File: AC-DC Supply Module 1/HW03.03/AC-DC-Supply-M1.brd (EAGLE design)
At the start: 125 x 100 mm, 76 parts, among them IC101 LD1117S33TR, IC102 TPS54202DDCR, IC103 TPS54202DDCR, IC104 MAX764CSA+, M101 M_HOLE_3M, M102 M_HOLE_3M, M103 M_HOLE_3M, M104 M_HOLE_3M, U101 TL431AQDBZR,215NEXPERIA_TL431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, X1 726386-2, X2 726386-2, X3 MOLEX_206832-0601MOLEX_206832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

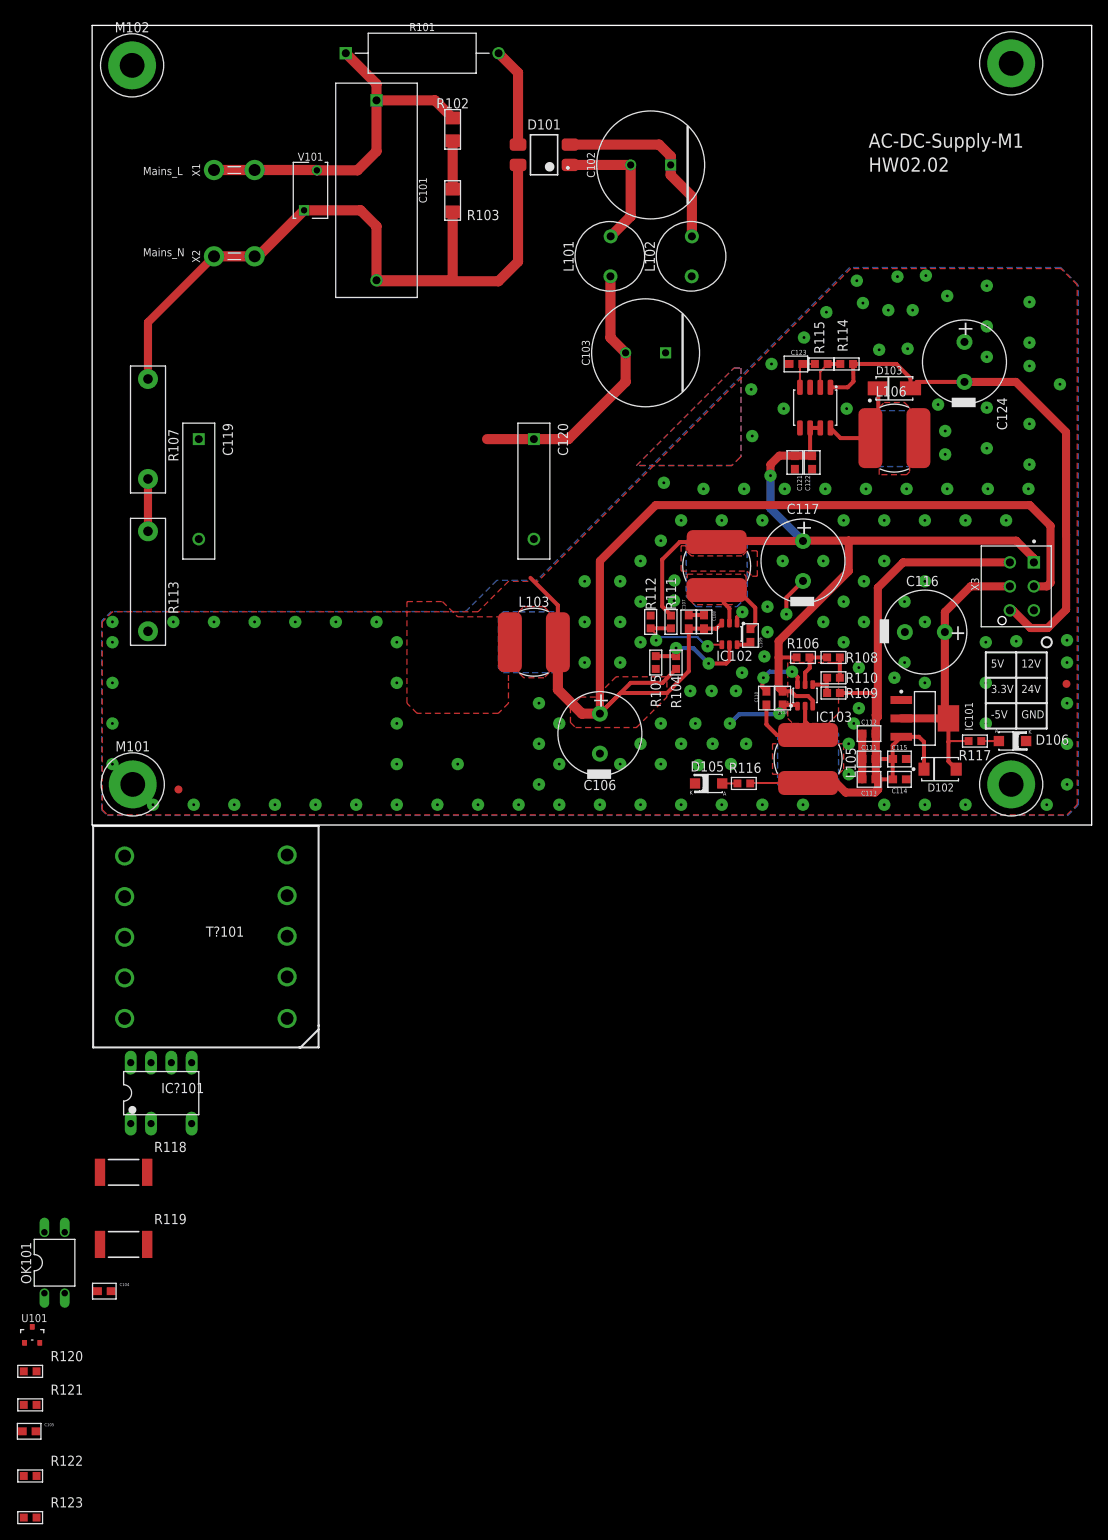
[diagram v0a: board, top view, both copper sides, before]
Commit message: HW03.03
Modified the AC/DC converter to a Flyback with custome transformer (Higher Power)
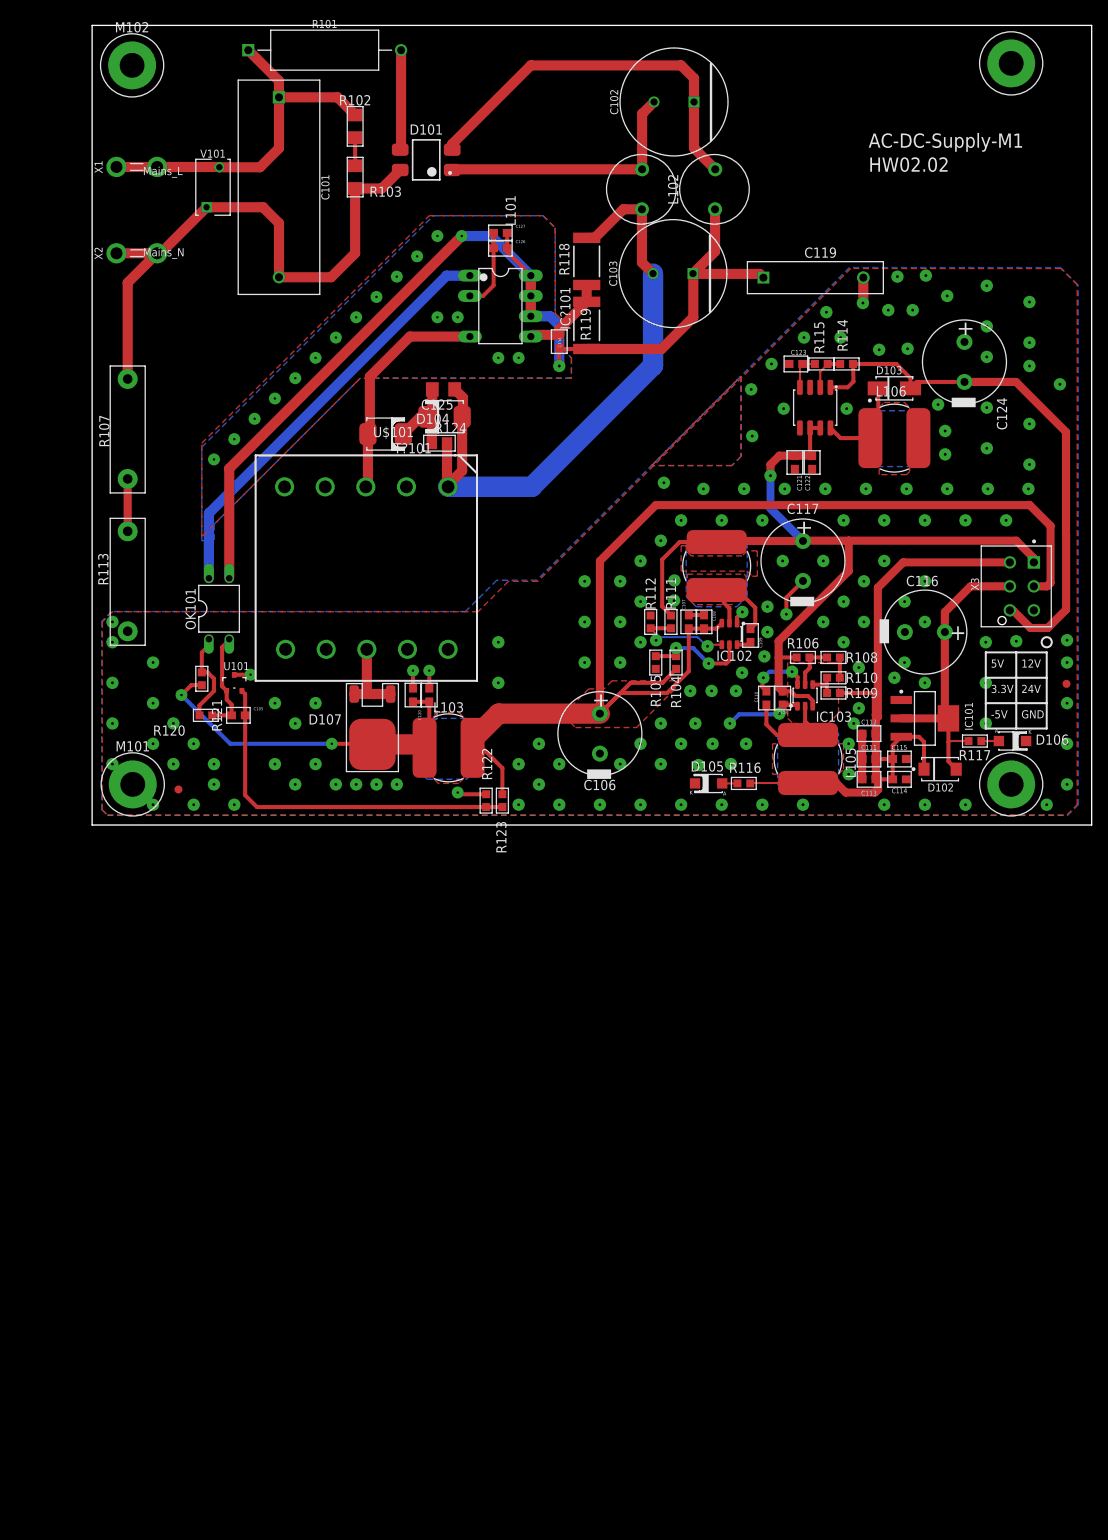
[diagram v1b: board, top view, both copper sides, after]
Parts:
- added C125: MCASS31QHB7102KTNA01, rcl:C1206
- added C126, C127: 100nF/50V, Labops_Lib_AH:0603
- added C128: 1uF/35V, Labops_Lib_AH:0603
- added D104: STTH1R04USMB, Labops_Lib_AH:SMB
- added D107: STTH1003SB-TR, Labops_Lib_AH:DPAK
- added R124: ERA-8AEB124V, Labops_Lib_AH:R0805
- added U$101: P6SMB120AT3GSMB, Labops_Lib_AH:SMB
- C120: value ERP610W471MEF0 -> 1uF/35V; device Labops_Lib_AH:CAP-P12.5-H15-W4-D1 -> Labops_Lib_AH:0603
- moved C104 131.7 mm to (58.4, 60.5), turned to 270 degrees
- moved R119 128.7 mm to (61.8, 62.5), turned to 90 degrees
- moved R118 127.8 mm to (61.8, 70.5), turned to 90 degrees
- moved IC?101 107.2 mm to (51.1, 64.9), turned to 270 degrees
- moved R123 106.3 mm to (49.3, 3.05), turned to 270 degrees
- moved R122 103.1 mm to (51.3, 3.05), turned to 90 degrees
- moved R121 93.3 mm to (13.7, 18.3), turned to 270 degrees
- moved C105 93.3 mm to (18.3, 13.7)
- moved U101 85.4 mm to (17.8, 17.8)
- moved R120 84.9 mm to (14.2, 13.7), turned to 180 degrees
- moved OK101 84.3 mm to (15.9, 27.1)
- moved C119 73.4 mm to (83.9, 68.5), turned to 0 degrees
- moved T?101 50.3 mm to (34.3, 32.1), turned to 90 degrees
- moved C120 35.4 mm to (40.1, 16.3)
- moved L103 17.0 mm to (44.6, 9.65)
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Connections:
- removed net 10_AC-DC_SUPPLY:VCC: IC?101.2
- new net 10_AC-DC_SUPPLY:N$29: C125.2, D104.K, R124.1, U$101.K
- new net 10_AC-DC_SUPPLY:V_RECT_F_MINUS: C103.1, C104.2, C119.P$1, C126.2, C127.2, IC?101.6, IC?101.7, IC?101.8, L102.2, OK101.3, R119.1
- net 10_AC-DC_SUPPLY:N$11: now also C126.1, C127.1, IC?101.2; no longer L103.1, R121.2, T?101.8
- net 10_AC-DC_SUPPLY:N$22: now also D104.A
- net 10_AC-DC_SUPPLY:N$23: now also D107.1, D107.3, T?101.8; no longer C120.P$2
- net 10_AC-DC_SUPPLY:N$24: now also C120.2, C128.2, D107.2, L103.1, R121.2; no longer C103.1, C104.2, IC?101.6, IC?101.7, IC?101.8, L102.2, OK101.3, R119.1
- net 10_AC-DC_SUPPLY:N$7: now also C125.1, R124.2, U$101.A; no longer C120.P$1
- net 10_AC-DC_SUPPLY:N$8: no longer R123.1
- net GND: now also C119.P$2, C120.1, C128.1, R123.1
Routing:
- net 10_AC-DC_SUPPLY:V_RECT_F_MINUS: track 0.00 -> 135.6 mm, vias 0 -> 18
- net 10_AC-DC_SUPPLY:N$26: track 0.00 -> 53.1 mm
- net 10_AC-DC_SUPPLY:N$8: track 0.00 -> 46.0 mm
- net 10_AC-DC_SUPPLY:N$7: track 34.3 -> 79.2 mm
- net 10_AC-DC_SUPPLY:N$24: track 0.00 -> 44.0 mm, vias 0 -> 2
- net 10_AC-DC_SUPPLY:N$22: track 0.00 -> 28.6 mm
- net N$2: track 98.0 -> 73.0 mm
- net 10_AC-DC_SUPPLY:N$6: track 24.3 -> 48.2 mm
- net 10_AC-DC_SUPPLY:N$5: track 17.6 -> 32.8 mm
- net GND: track 26.8 -> 40.1 mm, vias 151 -> 157
- net 10_AC-DC_SUPPLY:N$27: track 0.00 -> 12.8 mm
- net 10_AC-DC_SUPPLY:N$28: track 0.00 -> 11.7 mm
- net 10_AC-DC_SUPPLY:N$25: track 0.00 -> 11.3 mm
- net 10_AC-DC_SUPPLY:N$29: track 0.00 -> 11.1 mm
- net 10_AC-DC_SUPPLY:N$23: track 0.00 -> 10.2 mm
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- added copper zone on layer 1, net 10_AC-DC_SUPPLY:V_RECT_F_MINUS
- added copper zone on layer 16, net 10_AC-DC_SUPPLY:V_RECT_F_MINUS
- removed copper zone on layer 1, net 10_AC-DC_SUPPLY:N$11

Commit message: HW03.03
Done
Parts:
- added FID103: FIDUCIAL, Labops_Lib_AH:FIDUCIAL
- moved FID101 80.8 mm to (122.4, 98.4)
- moved FID102 9.25 mm to (1.91, 1.91)
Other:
- board text added: "HW03.03"
- board text removed: "HW02.02"
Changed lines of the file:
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@@
 <drawing>
 <settings>
-<setting alwaysvectorfont="no"/>
+<setting alwaysvectorfont="yes"/>
 <setting verticaltext="up"/>
 </settings>
-<grid distance="20" unitdist="mil" unit="mil" style="lines" multiple="5" display="yes" altdistance="20" altunitdist="mil" altunit="mil"/>
+<grid distance="5" unitdist="mil" unit="mil" style="lines" multiple="5" display="yes" altdistance="20" altunitdist="mil" altunit="mil"/>
 <layers>
 <layer number="1" name="Top" color="4" fill="1" visible="yes" active="yes"/>
@@
 <text x="6.35" y="71.12" size="1.016" layer="21">Mains_N</text>
 <text x="97.1" y="84.7" size="1.778" layer="21">AC-DC-Supply-M1</text>
-<text x="97.1" y="81.7" size="1.778" layer="21">HW02.02</text>
+<text x="97.1" y="81.7" size="1.778" layer="21">HW03.03</text>
 </plain>
 <attributes>
@@
 <attribute name="VERIFICATION_VERSION" value="0.0.0.3" x="106.045" y="6.985" size="1.778" layer="27" display="off"/>
 </element>
-<element name="FID101" library="Labops_Lib_AH" package="FIDUCIAL" value="FIDUCIAL" x="121.852" y="17.652" smashed="yes"/>
+<element name="FID101" library="Labops_Lib_AH" package="FIDUCIAL" value="FIDUCIAL" x="122.428" y="98.425" smashed="yes"/>
 <element name="IC101" library="Labops_Lib_AH" package="SOT223_LD1117S33TR" value="LD1117S33TR" x="104.14" y="13.335" smashed="yes">
 <attribute name="DESCRIPTION" value="LDO,Fixed 15V 3.3V 1.3V @ 800mA SOT-223 " x="104.14" y="13.335" size="1.778" layer="27" display="off"/>
@@
 <attribute name="VALUE" x="17.272" y="46.863" size="1.27" layer="27" font="vector" rot="R270" display="off"/>
 </element>
-<element name="FID102" library="Labops_Lib_AH" package="FIDUCIAL" value="FIDUCIAL" x="10.795" y="4.445" smashed="yes"/>
+<element name="FID102" library="Labops_Lib_AH" package="FIDUCIAL" value="FIDUCIAL" x="1.905" y="1.905" smashed="yes"/>
 <element name="D105" library="Labops_Lib_AH" package="SMD1206-LED" value="26-21/GPC-F3138B/CA" x="77.1" y="5.2" smashed="yes" rot="R180">
 <attribute name="DESCRIPTION" value="Green SMD LED 1206, 160mcd" x="77.1" y="5.2" size="1.778" layer="27" rot="R180" display="off"/>
@@
 <attribute name="VALUE" x="40.259" y="16.891" size="0.381" layer="27" rot="R270"/>
 </element>
+<element name="FID103" library="Labops_Lib_AH" package="FIDUCIAL" value="FIDUCIAL" x="122.428" y="1.905" smashed="yes"/>
 </elements>
 <signals>
@@
 <via x="2.54" y="12.7" extent="1-16" drill="0.35"/>
 <via x="2.54" y="7.62" extent="1-16" drill="0.35"/>
-<via x="7.62" y="2.54" extent="1-16" drill="0.35"/>
+<via x="11.938" y="5.588" extent="1-16" drill="0.35"/>
 <via x="12.7" y="2.54" extent="1-16" drill="0.35"/>
 <via x="15.24" y="5.08" extent="1-16" drill="0.35"/>

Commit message: HW03.03 Finished
This Version switches to Flyback converter for the AC/DC Part
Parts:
- C126: value 100nF/50V -> 1u/35V
- R122: value 40.2K 1% -> 33K 1%
- R123: value 4.7K 1% -> 3.9K 1%
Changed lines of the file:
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@@
 <drawing>
 <settings>
-<setting alwaysvectorfont="yes"/>
+<setting alwaysvectorfont="no"/>
 <setting verticaltext="up"/>
 </settings>
@@
 <layer number="23" name="tOrigins" color="15" fill="1" visible="yes" active="yes"/>
 <layer number="24" name="bOrigins" color="15" fill="1" visible="yes" active="yes"/>
-<layer number="25" name="tNames" color="7" fill="1" visible="no" active="yes"/>
+<layer number="25" name="tNames" color="7" fill="1" visible="yes" active="yes"/>
 <layer number="26" name="bNames" color="7" fill="1" visible="no" active="yes"/>
 <layer number="27" name="tValues" color="7" fill="1" visible="no" active="yes"/>
@@
 <attribute name="VALUE" x="17.653" y="11.811" size="0.381" layer="27"/>
 </element>
-<element name="R122" library="Labops_Lib_AH" package="EIA0603" value="40.2K 1%" x="51.308" y="3.048" smashed="yes" rot="R90">
+<element name="R122" library="Labops_Lib_AH" package="EIA0603" value="33K 1%" x="51.308" y="3.048" smashed="yes" rot="R90">
 <attribute name="DESCRIPTION" value="" x="51.308" y="3.048" size="1.778" layer="27" rot="R90" display="off"/>
 <attribute name="MFN" value="Open Source 0603" x="51.308" y="3.048" size="1.778" layer="27" rot="R90" display="off"/>
@@
 <attribute name="VALUE" x="52.832" y="5.588" size="1.27" layer="27" font="vector" rot="R90"/>
 </element>
-<element name="R123" library="Labops_Lib_AH" package="EIA0603" value="4.7K 1%" x="49.276" y="3.048" smashed="yes" rot="R270">
+<element name="R123" library="Labops_Lib_AH" package="EIA0603" value="3.9K 1%" x="49.276" y="3.048" smashed="yes" rot="R270">
 <attribute name="DESCRIPTION" value="" x="49.276" y="3.048" size="1.778" layer="27" rot="R270" display="off"/>
 <attribute name="MFN" value="Open Source 0603" x="49.276" y="3.048" size="1.778" layer="27" rot="R270" display="off"/>
@@
 <attribute name="VALUE" x="40.259" y="52.578" size="1.27" layer="27" font="vector" rot="R180"/>
 </element>
-<element name="C126" library="Labops_Lib_AH" package="0603" value="100nF/50V" x="51.054" y="72.136" smashed="yes">
+<element name="C126" library="Labops_Lib_AH" package="0603" value="1u/35V" x="51.054" y="72.136" smashed="yes">
 <attribute name="DESCRIPTION" value="" x="51.054" y="72.136" size="1.778" layer="27" display="off"/>
 <attribute name="MFN" value="Open Source" x="51.054" y="72.136" size="1.778" layer="27" display="off"/>

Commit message: AC-DC Supply update
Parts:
- C125: value MCASS31QHB7102KTNA01 -> 220pF/1KV
- R123: value 3.9K 1% -> 5.6K 1%
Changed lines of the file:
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@@
 <attribute name="VALUE" x="52.832" y="5.588" size="1.27" layer="27" font="vector" rot="R90"/>
 </element>
-<element name="R123" library="Labops_Lib_AH" package="EIA0603" value="3.9K 1%" x="49.276" y="3.048" smashed="yes" rot="R270">
+<element name="R123" library="Labops_Lib_AH" package="EIA0603" value="5.6K 1%" x="49.276" y="3.048" smashed="yes" rot="R270">
 <attribute name="DESCRIPTION" value="" x="49.276" y="3.048" size="1.778" layer="27" rot="R270" display="off"/>
 <attribute name="MFN" value="Open Source 0603" x="49.276" y="3.048" size="1.778" layer="27" rot="R270" display="off"/>
@@
 <attribute name="VALUE" x="42.799" y="45.212" size="1.27" layer="27"/>
 </element>
-<element name="C125" library="rcl" library_urn="urn:adsk.eagle:library:334" package="C1206" package3d_urn="urn:adsk.eagle:package:23618/2" value="MCASS31QHB7102KTNA01" x="43.942" y="54.483" smashed="yes" rot="R180">
+<element name="C125" library="rcl" library_urn="urn:adsk.eagle:library:334" package="C1206" package3d_urn="urn:adsk.eagle:package:23618/2" value="220pF/1KV" x="43.942" y="54.483" smashed="yes" rot="R180">
 <attribute name="NAME" x="45.212" y="53.213" size="1.27" layer="25" rot="R180"/>
 <attribute name="POPULARITY" value="54" x="43.942" y="54.483" size="1.778" layer="27" rot="R180" display="off"/>
